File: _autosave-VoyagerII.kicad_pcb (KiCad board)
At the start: 2 copper layers, 285 x 94.6 mm, 268 parts, among them P1 TC2030-IDC, SW1 SW_PUSH, U1 ATXMEGA32A4U-AU, U2 MCP1700T-3002E/TT, U3 PRTR5V0U2X, U4 IS31FL3731-SALS2, U5 74LVC1G34

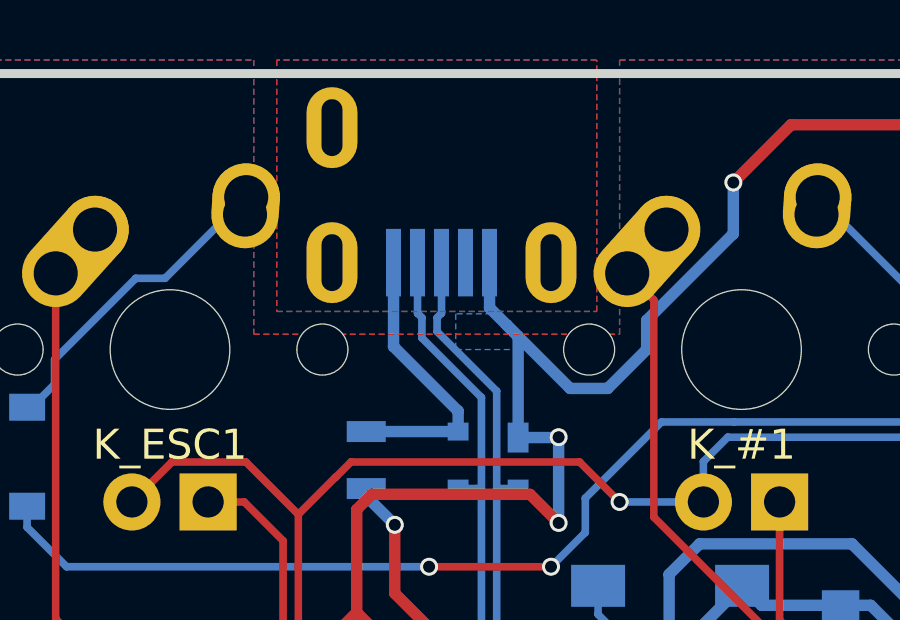
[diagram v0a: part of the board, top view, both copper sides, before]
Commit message: Move USB setup
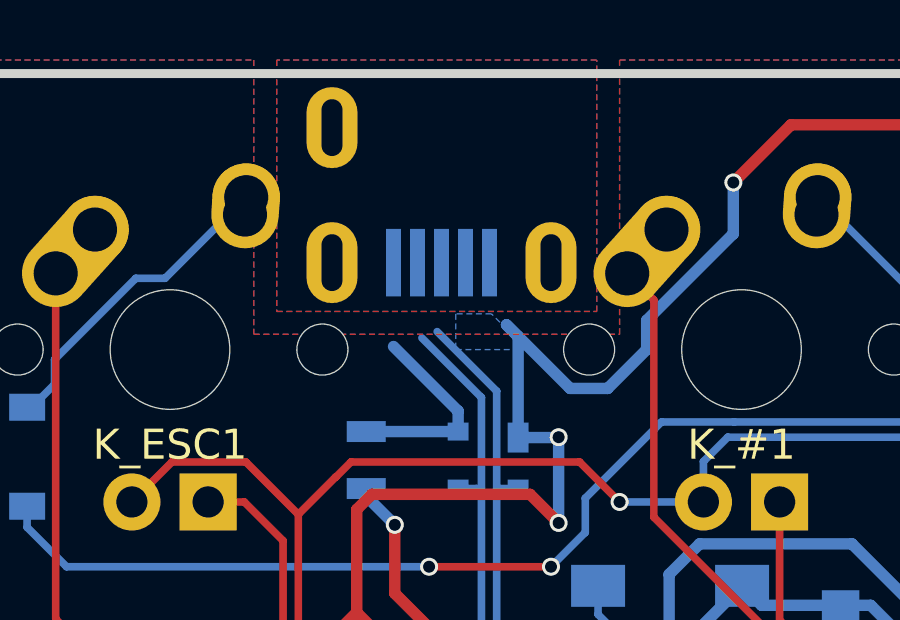
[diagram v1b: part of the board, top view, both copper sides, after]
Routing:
- net VCC: track 9.59 -> 6.79 mm
- net D-: track 140.3 -> 137.7 mm
- net D+: track 140.3 -> 137.9 mm
- net GND: track 958.3 -> 956.0 mm
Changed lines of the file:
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@@
   (general
     (links 659)
-    (no_connects 18)
-    (area 0 0 0 0)
+    (no_connects 4)
+    (area 46.495049 28.25625 334.554951 153.909376)
     (thickness 1.6)
     (drawings 35)
-    (tracks 3001)
+    (tracks 2992)
     (zones 0)
     (modules 268)
@@
   (segment (start 188.976 124.714) (end 207.01 124.714) (width 0.381) (layer F.Cu) (net 2))
   (segment (start 211.150906 121.580544) (end 211.150906 113.328892) (width 0.381) (layer F.Cu) (net 2))
-  (segment (start 67.8 54.25225) (end 67.8 55.75825) (width 0.381) (layer B.Cu) (net 2) (status 10))
   (segment (start 63.881 61.976) (end 69.1515 61.976) (width 0.381) (layer F.Cu) (net 2))
   (segment (start 69.1515 61.976) (end 70.104 62.9285) (width 0.381) (layer F.Cu) (net 2))
@@
   (via (at 70.104 60.071) (size 0.6) (drill 0.4) (layers F.Cu B.Cu) (net 2))
   (segment (start 68.36625 56.3245) (end 70.487151 58.445401) (width 0.381) (layer B.Cu) (net 2))
-  (segment (start 67.8 55.75825) (end 68.36625 56.3245) (width 0.381) (layer B.Cu) (net 2))
   (segment (start 68.36625 56.3245) (end 68.7545 56.71275) (width 0.381) (layer B.Cu) (net 2))
   (segment (start 68.7545 56.71275) (end 68.7545 60.083) (width 0.381) (layer B.Cu) (net 2) (status 20))
@@
   (via (at 153.83404 137.460048) (size 0.6) (drill 0.4) (layers F.Cu B.Cu) (net 3))
   (segment (start 66.7545 59.883) (end 63.6905 59.883) (width 0.381) (layer B.Cu) (net 4) (status 30))
-  (segment (start 64.6 57.0475) (end 64.6 54.25225) (width 0.381) (layer B.Cu) (net 4) (status 20))
   (segment (start 66.7545 59.883) (end 66.7545 59.202) (width 0.381) (layer B.Cu) (net 4) (status 10))
   (segment (start 66.7545 59.202) (end 64.6 57.0475) (width 0.381) (layer B.Cu) (net 4))
@@
   (segment (start 68.707 77.82921) (end 68.707 75.41621) (width 0.254) (layer B.Cu) (net 27))
   (segment (start 68.707 75.41621) (end 67.531 74.24021) (width 0.254) (layer B.Cu) (net 27))
-  (segment (start 65.4 54.25225) (end 65.4 55.93975) (width 0.254) (layer B.Cu) (net 27) (status 10))
-  (segment (start 65.4 55.93975) (end 65.546 56.08575) (width 0.254) (layer B.Cu) (net 27))
-  (segment (start 65.546 56.08575) (end 65.546 56.76121) (width 0.254) (layer B.Cu) (net 27))
   (segment (start 68.039 58.53579) (end 68.039 61.7855) (width 0.254) (layer B.Cu) (net 28))
   (segment (start 68.039 61.7855) (end 68.039 74.02979) (width 0.254) (layer B.Cu) (net 28))
@@
   (segment (start 68.0415 61.783) (end 68.039 61.7855) (width 0.254) (layer B.Cu) (net 28))
   (segment (start 77.19421 85.598) (end 133.45521 85.598) (width 0.254) (layer B.Cu) (net 28))
-  (segment (start 66.2 54.25225) (end 66.2 55.93975) (width 0.254) (layer B.Cu) (net 28) (status 10))
-  (segment (start 66.2 55.93975) (end 66.054 56.08575) (width 0.254) (layer B.Cu) (net 28))
   (segment (start 147.193 116.94521) (end 144.5325 119.60571) (width 0.254) (layer B.Cu) (net 28))
-  (segment (start 66.054 56.08575) (end 66.054 56.55079) (width 0.254) (layer B.Cu) (net 28))
   (segment (start 66.054 56.55079) (end 68.039 58.53579) (width 0.254) (layer B.Cu) (net 28))
   (segment (start 68.039 74.02979) (end 69.215 75.20579) (width 0.254) (layer B.Cu) (net 28))
